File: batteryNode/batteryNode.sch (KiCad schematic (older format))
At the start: 32 parts

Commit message: updatedSchem
changes some more small things
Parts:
- added C? (x2): 1u, symbol Device:C_Small
- added C? (x4): .1u, symbol Device:C_Small
- added D?: LED, symbol Device:LED
- added R? (x3): R, symbol Device:R
- added R?: 10k, symbol Device:R
- added SW?: SW_Push, symbol Switch:SW_Push
- added U?: LTC2875-DD, Package_DFN_QFN:DFN-8-1EP_3x3mm_P0.5mm_EP1.66x2.38mm, symbol Interface_CAN_LIN:LTC2875-DD
- R? (x7): value R -> 100
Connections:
- net +3V3: now also C?.1, C?.1, C?.1, C?.1, C?.1, C?.1, R?.1, R?.1, U?.3 (VCC)
- net GND: now also C?.2, C?.2, C?.2, C?.2, C?.2, C?.2, D?.1 (K), R?.2, SW?.2, U?.2 (GND), U?.9 (GND)
- net RXD: now also U?.4 (RXD)
- net TXD: now also U?.1 (TXD)
- net ~alert: now also U?.4 (PD2), R?.2
- net ~reset: now also SW?.1
- new net: R?.1, R?.2, U?.8 (RS)
- new net: D?.2 (A), R?.2
- new net indicatorLED: R?.1
- no-connect marks 6 -> 7

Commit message: modified schem
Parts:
- U1: renamed from U?; footprint (none) -> Package_DFN_QFN:VQFN-24-1EP_4x4mm_P0.5mm_EP2.45x2.45mm_ThermalVias
- gave numbers to parts that had none: 44
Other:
- moved on the sheet: C1, C10, C11, C12, C13, C14, C15, C17, C18, C2, C3, C4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

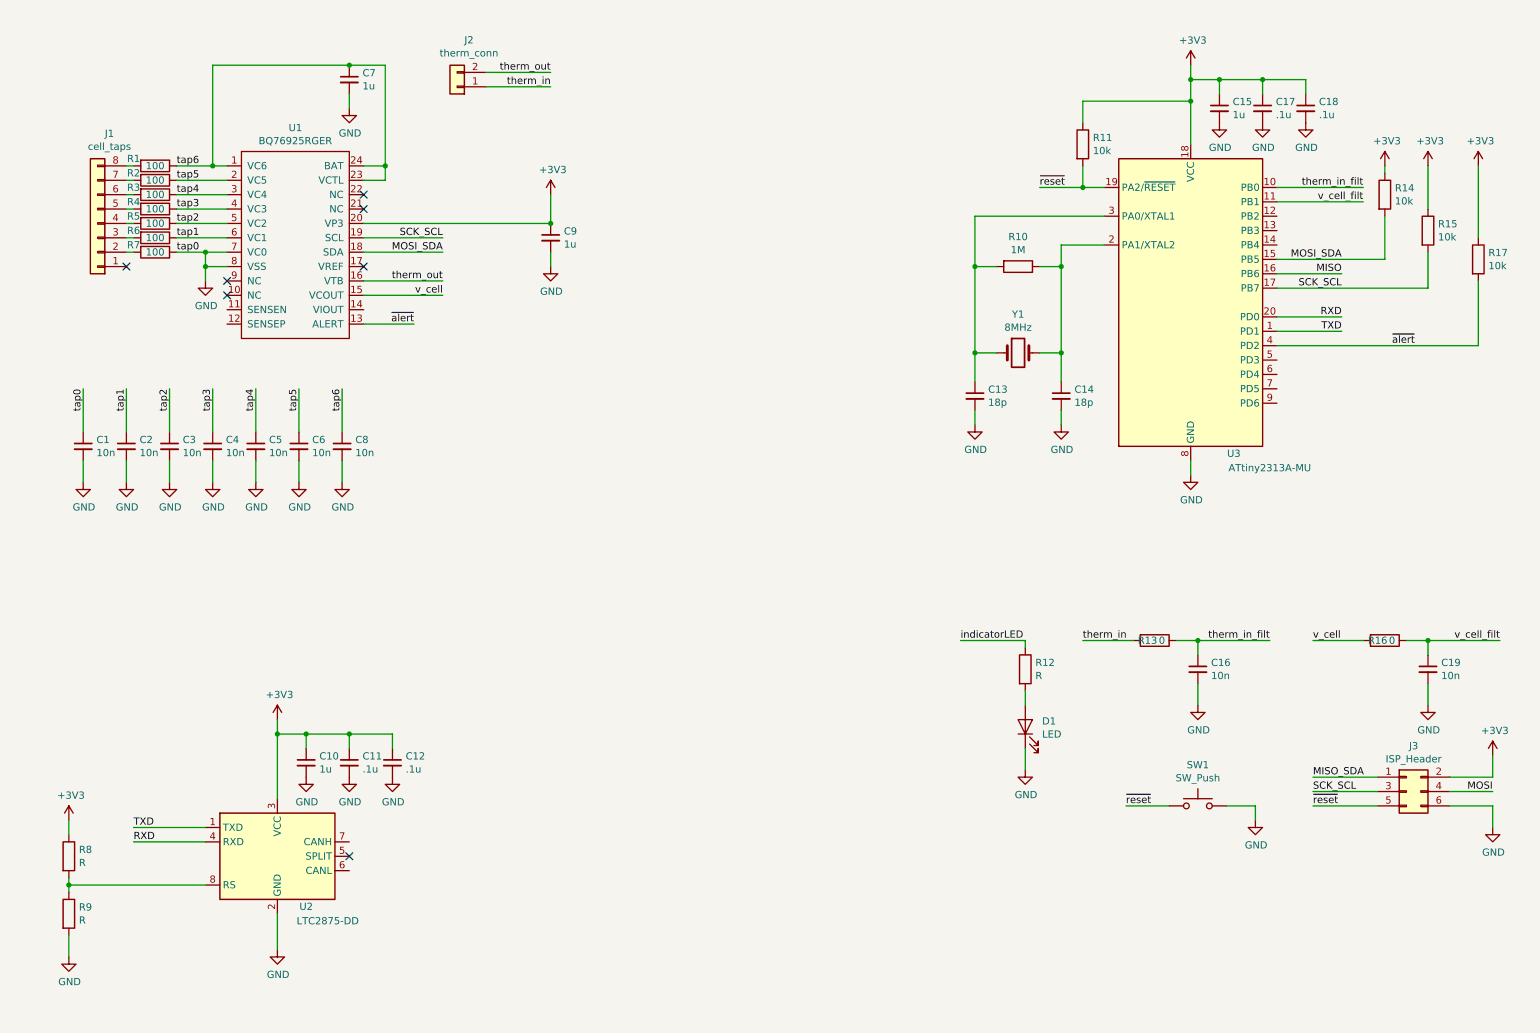
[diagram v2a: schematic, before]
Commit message: Added some footprints and digikey part numbers
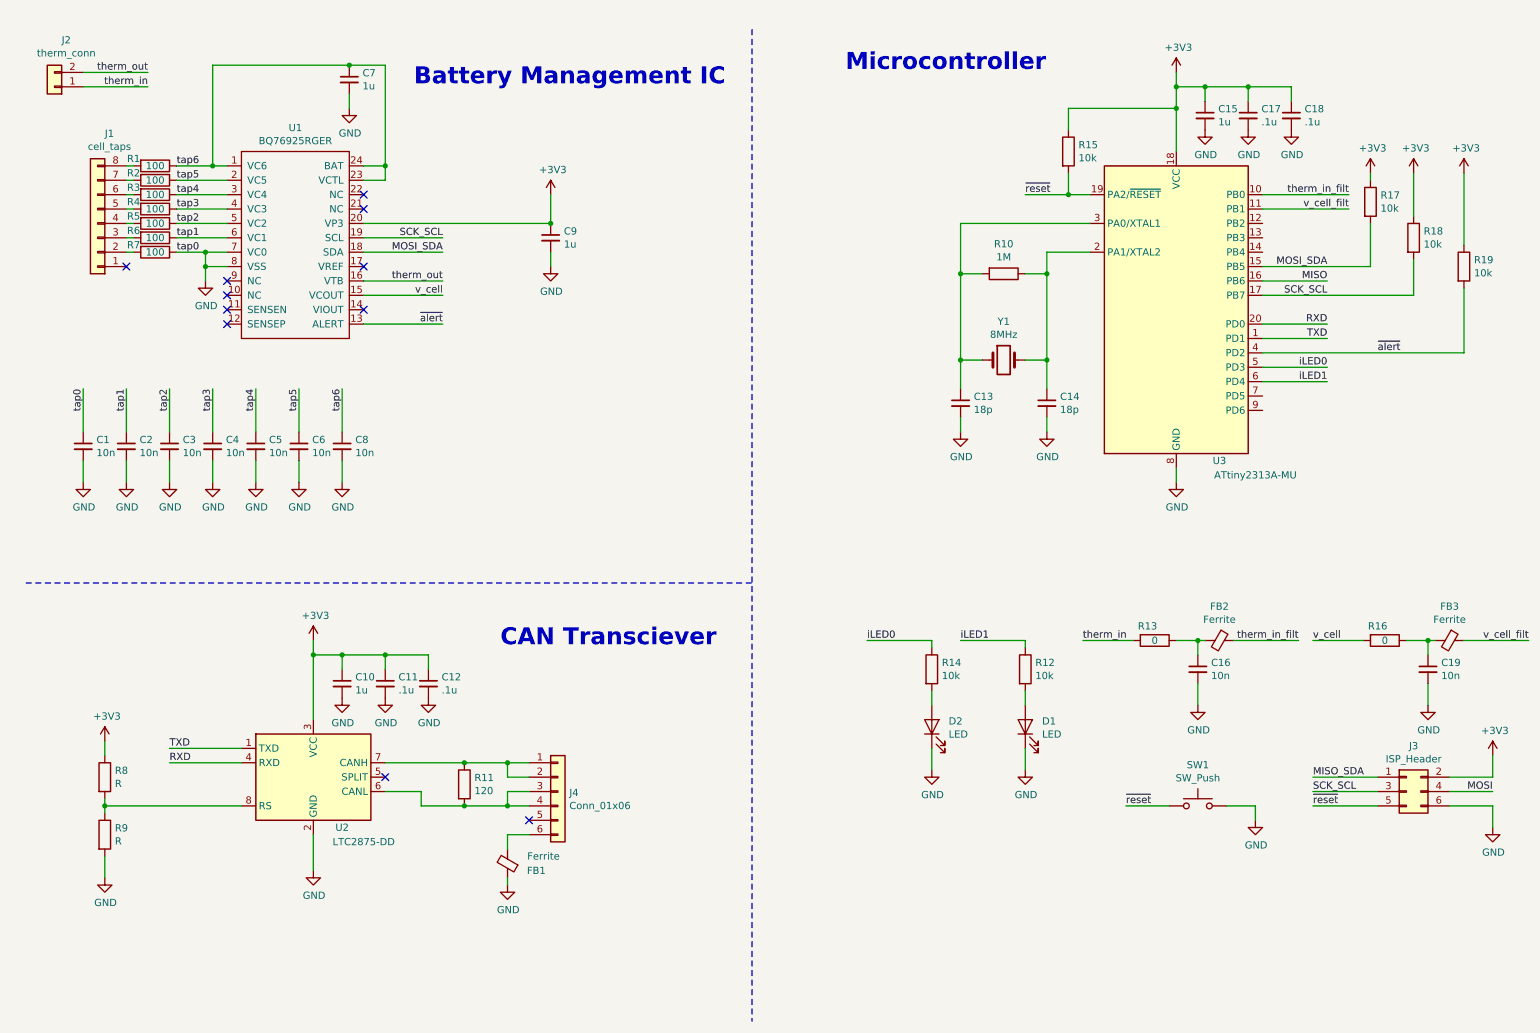
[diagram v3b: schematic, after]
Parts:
- added D2: LED, LED_SMD:LED_0603_1608Metric, symbol Device:LED
- added FB1: Ferrite, symbol Device:Ferrite_Bead_Small
- added FB2, FB3: Ferrite, Inductor_SMD:L_0603_1608Metric, symbol Device:Ferrite_Bead_Small
- added J4: Conn_01x06, symbol Connector_Generic:Conn_01x06
- added R18, R19: 10k, Resistor_SMD:R_0603_1608Metric, symbol Device:R
- C16, C19, R10: footprint (none) -> Capacitor_SMD:C_0603_1608Metric
- D1: footprint (none) -> LED_SMD:LED_0603_1608Metric
- J3: footprint (none) -> Connector_PinHeader_1.27mm:PinHeader_2x03_P1.27mm_Vertical
- R11: value 10k -> 120
- R12: value R -> 10k; footprint (none) -> Resistor_SMD:R_0603_1608Metric
- R13, R14, R15, R16, R17: footprint (none) -> Resistor_SMD:R_0603_1608Metric
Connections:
- net indicatorLED is gone; now on net iLED1: R12.1
- net +3V3: now also R18.1, R19.1; no longer R11.1, R14.1
- net GND: now also D2.1 (K), FB1.1
- net MOSI_SDA: now also R17.2; no longer R14.2
- net SCK_SCL: now also R18.2; no longer R15.2
- net therm_in_filt: now also FB2.1; no longer C16.1, R13.1
- net v_cell_filt: now also FB3.1; no longer C19.1, R16.1
- net ~alert: now also R19.2; no longer R17.2
- net ~reset: now also R15.2; no longer R11.2
- net iLED0: now reaches U3.5 (PD3)
- net iLED0: now also R14.1
- net iLED1: now reaches U3.6 (PD4)
- net at U2.6 (CANL): now also R11.2, J4.3 (Pin_3), J4.4 (Pin_4)
- net at U2.7 (CANH): now also R11.1, J4.1 (Pin_1), J4.2 (Pin_2)
- new net: C16.1, FB2.2, R13.1
- new net: C19.1, FB3.2, R16.1
- new net: FB1.2, J4.6 (Pin_6)
- new net: D2.2 (A), R14.2
- no-connect marks 7 -> 11
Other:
- note added: "Battery Management IC"
- note added: "CAN Transciever\n"
- note added: "Microcontroller\n"
- moved on the sheet: C10, C11, C12, C13, C14, C15, C17, C18, J2, R10, R8, R9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

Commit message: Schematic Complete
V 0.1 of schematic complete. Trial layout next
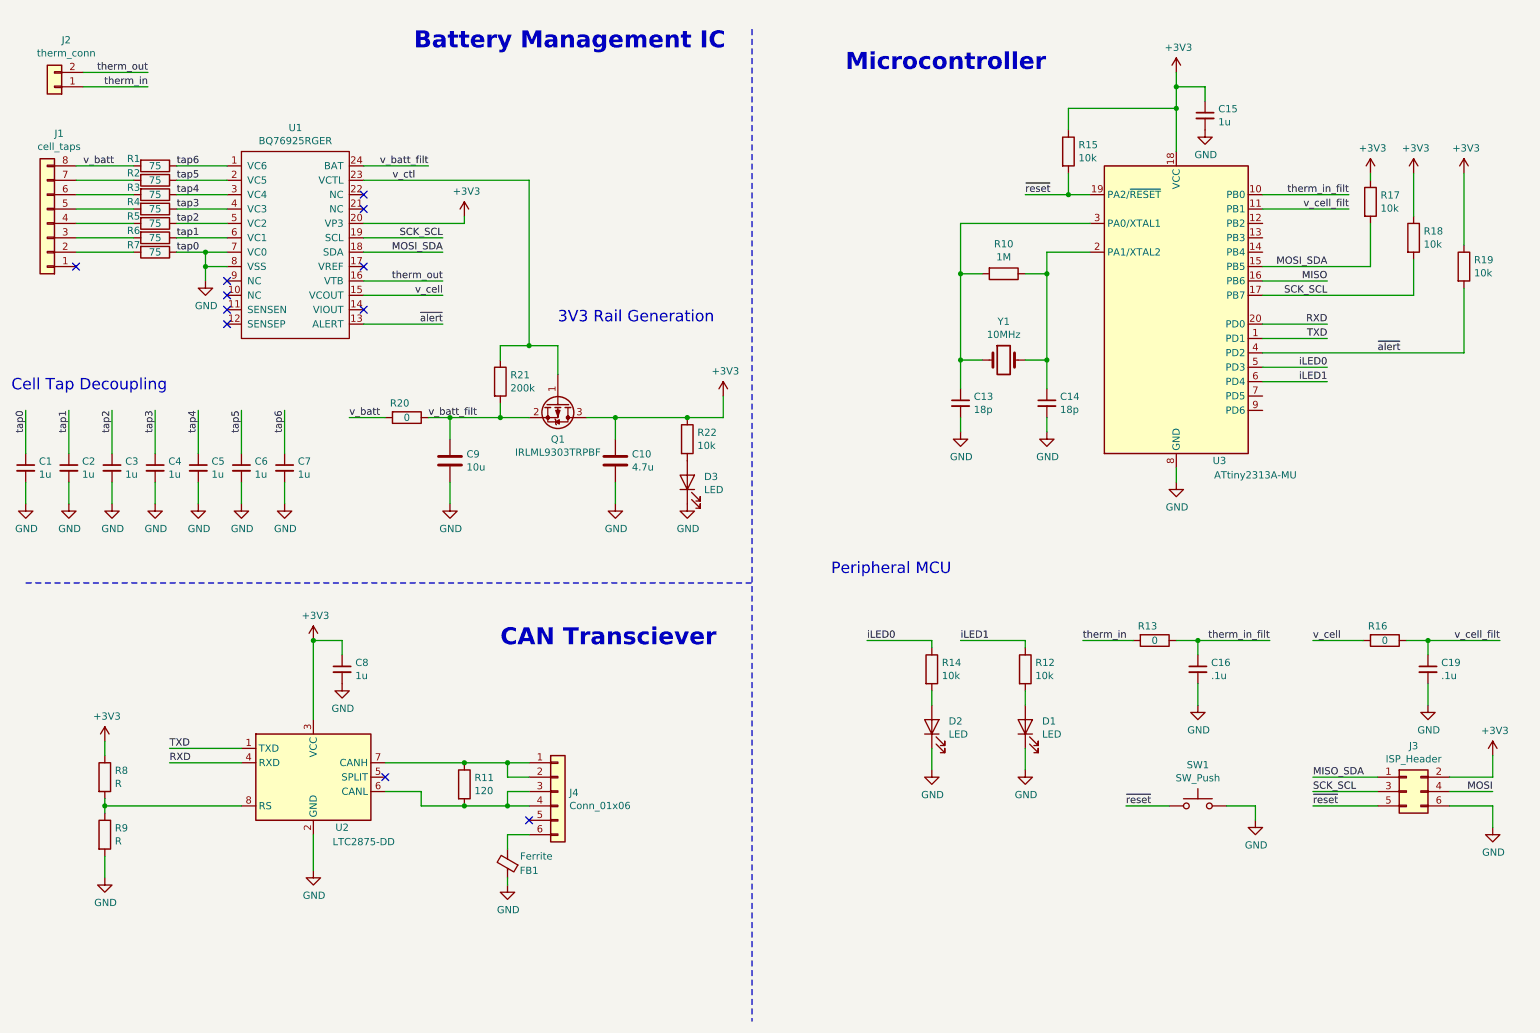
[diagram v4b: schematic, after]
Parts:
- removed C10, C9: 1u, symbol Device:C_Small
- removed C11, C12, C17, C18: .1u, symbol Device:C_Small
- removed FB2, FB3: Ferrite, Inductor_SMD:L_0603_1608Metric, symbol Device:Ferrite_Bead_Small
- added C10: 4.7u, Capacitor_SMD:C_0603_1608Metric_Pad1.05x0.95mm_HandSolder, symbol Device:C
- added C9: 10u, Capacitor_SMD:C_0603_1608Metric_Pad1.05x0.95mm_HandSolder, symbol Device:C
- added D3: LED, LED_SMD:LED_0603_1608Metric, symbol Device:LED
- added Q1: IRLML9303TRPBF, Package_TO_SOT_SMD:SOT-23, symbol Device:Q_PMOS_GSD
- added R20: 0, Resistor_SMD:R_0603_1608Metric, symbol Device:R
- added R21: 200k, Resistor_SMD:R_0603_1608Metric, symbol Device:R
- added R22: 10k, Resistor_SMD:R_0603_1608Metric, symbol Device:R
- C1, C2, C3, C4, C5, C6, C8: value 10n -> 1u; footprint (none) -> Capacitor_SMD:C_0603_1608Metric
- C13, C14: footprint (none) -> Capacitor_SMD:C_0402_1005Metric
- C15, C7: footprint (none) -> Capacitor_SMD:C_0603_1608Metric
- C16, C19: value 10n -> .1u
- FB1: footprint (none) -> Inductor_SMD:L_0603_1608Metric
- J1: footprint (none) -> Connector_Molex:Molex_Mini-Fit_Jr_5569-08A2_2x04_P4.20mm_Horizontal
- J2: footprint (none) -> Connector_Molex:Molex_Mini-Fit_Jr_5569-02A2_2x01_P4.20mm_Horizontal
- J4: footprint (none) -> Connector_Molex:Molex_Mini-Fit_Jr_5569-06A2_2x03_P4.20mm_Horizontal
- R1, R2, R3, R4, R5, R6, R7: value 100 -> 75; footprint (none) -> Resistor_SMD:R_0805_2012Metric
- R11, R8, R9: footprint (none) -> Resistor_SMD:R_0603_1608Metric
- SW1: footprint (none) -> Button_Switch_SMD:SW_SPST_EVQPE1
- Y1: value 8MHz -> 10MHz; footprint (none) -> BMSLib:ECS-100-18-23G-JGN-TR
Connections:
- net +3V3: now also C8.1, C10.1, Q1.3 (D), R22.1
- net GND: now also C10.2, C9.2, D3.1 (K)
- net tap6: no longer C8.1, U1.23 (VCTL), U1.24 (BAT)
- net therm_in_filt: now also C16.1, R13.1
- net v_cell_filt: now also C19.1, R16.1
- net v_batt: now reaches J1.8 (Pin_8), R1.2
- net v_batt: now also R20.2
- new net: D3.2 (A), R22.2
- new net v_batt_filt: C9.1, Q1.2 (S), R20.1, R21.2, U1.24 (BAT)
- new net v_ctl: Q1.1 (G), R21.1, U1.23 (VCTL)
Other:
- note added: "3V3 Rail Generation\n"
- note added: "Cell Tap Decoupling\n\n"
- note added: "Peripheral MCU \n"
- moved on the sheet: C1, J1

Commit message: Terrible First Version Layout
First version layout. Going to try some routing with this and see how it works out.
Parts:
- renumbered C1 to C101, C2 to C102, C3 to C103, C4 to C104, C5 to C105, C6 to C106, C7 to C107, C9 to C108, C10 to C109, C15 to C200, C13 to C201, C14 to C202, C16 to C203, C19 to C204, C8 to C300, D3 to D10, D2 to D200, D1 to D201, FB1 to FB300, J1 to J100, J2 to J101, J3 to J200, J4 to J300, Q1 to Q100, R1 to R101, R2 to R102, R3 to R103, R4 to R104, R5 to R105, R6 to R106, R7 to R107, R20 to R108, R21 to R109, R22 to R110, R15 to R200, R17 to R201, R18 to R202, R19 to R203, R10 to R204, R14 to R205, R12 to R206, R13 to R207, R16 to R208, R8 to R300, R9 to R301, R11 to R302, SW1 to SW200, U1 to U100, U3 to U200, U2 to U300, Y1 to Y200
